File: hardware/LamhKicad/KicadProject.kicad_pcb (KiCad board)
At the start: 2 copper layers, 60 x 60 mm, 44 parts, among them J1 JTAG-10 PIN, J2 436500303, J3 436500303, J4 436500303, J5 ESQ-110-X-X-D, J6 436500303, U1 TJA1051T-3, U2 PCA9685PW_112, U3 TLV70433DBVT, U4 STM32F072C8Tx

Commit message: ready to route
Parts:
- added C16: 1000uf 16v, Capacitor_THT:CP_Radial_D10.0mm_P5.00mm, F.Cu at (184.0, 81.0)
- added C18: 1000uf 16v, Capacitor_THT:CP_Radial_D10.0mm_P5.00mm, F.Cu at (173.1, 90.2)
- added C19: 1000uf 16v, Capacitor_THT:CP_Radial_D10.0mm_P5.00mm, F.Cu at (194.8, 81.2)
- added C20: 1000uf 16v, Capacitor_THT:CP_Radial_D10.0mm_P5.00mm, F.Cu at (173.1, 101.0)
- moved R2 29.4 mm to (196.0, 90.9), turned to 90 degrees
- moved R1 25.8 mm to (197.0, 90.9), turned to 90 degrees
- moved R6 19.6 mm to (194.0, 90.9)
- moved R3 11.8 mm to (195.0, 90.9)
- moved JP1 10.1 mm to (204.2, 94.8)
- moved JP2 9.91 mm to (207.7, 95.5)
- moved JP3 9.91 mm to (204.2, 97.5)
- moved JP4 9.91 mm to (207.7, 98.2)
- moved R7 9.45 mm to (199.5, 102.2)
- moved R8 9.45 mm to (199.8, 101.2)
- moved C17 9.29 mm to (200.9, 99.6)
- moved R11 9.29 mm to (196.8, 100.5)
- moved U2 9.29 mm to (195.5, 96.0)
- moved C8 3.33 mm to (185.2, 101.0)
- moved C10 3.20 mm to (190.0, 112.4)
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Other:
- copper layers 2 -> 4

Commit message: Changes
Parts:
- moved C12 40.9 mm to (187.5, 94.6)
- moved C13 40.9 mm to (187.5, 96.1)
- moved C14 40.9 mm to (187.5, 98.0)
- moved C15 40.9 mm to (187.5, 100.0)
- moved R13 33.8 mm to (201.5, 97.0)
- moved R12 32.9 mm to (201.5, 96.0)
- moved R10 30.0 mm to (201.5, 95.0)
- moved R9 29.0 mm to (201.5, 94.0)
- moved C4 18.0 mm to (204.0, 110.0)
- moved C3 17.7 mm to (204.0, 108.5)
- moved C1 15.9 mm to (204.0, 107.1)
- moved C11 12.7 mm to (190.7, 112.4), turned to 0 degrees
- moved C10 12.7 mm to (184.3, 101.0)
- moved C9 9.53 mm to (190.7, 113.4), turned to 0 degrees
- moved C8 4.93 mm to (181.8, 104.5), turned to -90 degrees
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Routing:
- added copper zone on B.Cu, net GND
- added copper zone on F.Cu, net GND
- added copper zone on In1.Cu, net GND
- added copper zone on In2.Cu, net GND

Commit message: fixed the connector
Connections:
- J5 pad 12: NRST4 -> SWCLK4
- J5 pad 17: SWCLK -> NRST
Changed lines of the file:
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@@
 	(net 82 "Net-(JP3-B)")
 	(net 83 "Net-(JP4-B)")
+	(net 84 "NRST")
+	(net 85 "SWCLK4")
 	(footprint "Capacitor_SMD:C_0402_1005Metric"
 		(layer "F.Cu")
@@
 			(layers "*.Cu" "*.Mask")
 			(remove_unused_layers no)
-			(net 20 "NRST4")
+			(net 85 "SWCLK4")
 			(pinfunction "12")
 			(pintype "passive")
@@
 			(layers "*.Cu" "*.Mask")
 			(remove_unused_layers no)
-			(net 25 "SWCLK")
+			(net 84 "NRST")
 			(pinfunction "17")
 			(pintype "passive")

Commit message: minor changes
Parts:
- added R14: 10kΩ, Resistor_SMD:R_0402_1005Metric, F.Cu at (186.2, 101.0)
- added R15: 10kΩ, Resistor_SMD:R_0402_1005Metric, F.Cu at (179.0, 108.2)
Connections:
- U4 pad 44: unconnected-(U4-BOOT0-Pad44) -> Net-(U4-BOOT0)
- U4 pad 7: NRST4 -> NRST

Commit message: minor changes
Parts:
- removed R15: 10kΩ, Resistor_SMD:R_0402_1005Metric
- added C21: 100nF, Capacitor_SMD:C_0402_1005Metric, F.Cu at (184.2, 109.7)
- added C27: 8pF, Capacitor_SMD:C_0402_1005Metric, F.Cu at (181.2, 102.0)
- added C28: 8pF, Capacitor_SMD:C_0402_1005Metric, F.Cu at (180.2, 107.2)
- added G***: LOGO, LOGO, F.Cu at (196.3, 111.0)
- added G***: LOGO, LOGO, F.Cu at (185.8, 93.5)
- added XTAL1: NX3225GD-8MHZ-STD-CRA-3, footprints:XTAL_NX3225GD-8MHZ-STD-CRA-3_NDK, F.Cu at (181.2, 104.5)
- moved C12 14.8 mm to (182.0, 108.3), turned to 180 degrees
- moved R7 14.4 mm to (185.7, 98.2), turned to 0 degrees
- moved C13 14.3 mm to (182.0, 109.3), turned to 180 degrees
- moved R8 11.1 mm to (188.8, 99.2)
- moved C3 10.7 mm to (194.3, 104.0), turned to 90 degrees
- moved C4 10.6 mm to (195.3, 104.0), turned to 90 degrees
- moved C14 5.66 mm to (192.7, 100.2)
- moved C15 5.36 mm to (192.7, 101.2)
- moved C8 4.29 mm to (183.4, 100.5), turned to 90 degrees
- moved C7 4.26 mm to (182.4, 100.5), turned to 90 degrees
- moved C1 3.75 mm to (200.3, 107.2), turned to 180 degrees
- moved R6 2.85 mm to (191.2, 90.7), turned to 0 degrees
- moved C9 2.71 mm to (190.6, 110.7), turned to 180 degrees
- moved R14 2.48 mm to (187.2, 98.7), turned to 90 degrees
- moved U1 2.32 mm to (199.5, 103.9)
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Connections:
- J1 pad 1: NRST4 -> NRST
- J1 pad 2: SWCLK -> SWCLK4
- J5 pad 16: CAN_o+ -> CAN_+
- J5 pad 18: CAN_o- -> CAN_-
- R1 pad 1: Net-(J2-Pad1) -> Net-(J4-Pad1)
- R2 pad 1: Net-(J3-Pad1) -> Net-(J6-Pad1)
- R2 pad 2: Net-(U2-LED1) -> Net-(U2-LED2)
- R3 pad 1: Net-(J4-Pad1) -> Net-(J2-Pad1)
- R3 pad 2: Net-(U2-LED2) -> Net-(U2-LED4)
- R6 pad 1: Net-(J6-Pad1) -> Net-(J3-Pad1)
- R6 pad 2: Net-(U2-LED3) -> Net-(U2-LED6)
- U1 pad 1: CAN_+ -> CAN_e+
- U1 pad 4: CAN_- -> CAN_e-
- U2 pad 10: unconnected-(U2-LED4-Pad10) -> Net-(U2-LED4)
- U2 pad 12: unconnected-(U2-LED6-Pad12) -> Net-(U2-LED6)
- U2 pad 7: Net-(U2-LED1) -> unconnected-(U2-LED1-Pad7)
- U2 pad 9: Net-(U2-LED3) -> unconnected-(U2-LED3-Pad9)
- U4 pad 11: CS -> unconnected-(U4-PA1-Pad11)
- U4 pad 12: OE -> unconnected-(U4-PA2-Pad12)
- U4 pad 13: RESET -> unconnected-(U4-PA3-Pad13)
- U4 pad 14: ADC -> unconnected-(U4-PA4-Pad14)
- U4 pad 15: CLK -> unconnected-(U4-PA5-Pad15)
- U4 pad 16: MISO -> unconnected-(U4-PA6-Pad16)
- U4 pad 17: MOSI -> unconnected-(U4-PA7-Pad17)
- U4 pad 3: SWCLK -> SWCLK4
- U4 pad 32: CAN_- -> CAN_e-
- U4 pad 33: CAN_+ -> CAN_e+
- U4 pad 5: unconnected-(U4-PF0-Pad5) -> Net-(U4-PF0)
- U4 pad 6: unconnected-(U4-PF1-Pad6) -> Net-(U4-PF1)
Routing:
- net 3.3V: track 1.52 -> 122.9 mm, vias 0 -> 9
- net NRST: track 0.00 -> 69.0 mm, vias 0 -> 1
- net SWCLK4: track 0.00 -> 50.1 mm, vias 0 -> 1
- net SWDIO: track 0.00 -> 46.8 mm, vias 0 -> 1
- net Net-(J3-Pad1): track 0.00 -> 31.4 mm
- net Net-(J2-Pad1): track 0.00 -> 28.7 mm
- net Net-(J6-Pad1): track 0.00 -> 25.5 mm
- net SCL: track 0.00 -> 19.3 mm, vias 0 -> 2
- net GND: track 1.56 -> 19.9 mm, vias 0 -> 50
- net SDA: track 0.00 -> 17.8 mm, vias 0 -> 2
- net Net-(J4-Pad1): track 0.00 -> 17.7 mm
- net Net-(JP4-B): track 0.00 -> 14.1 mm
- net Net-(JP2-B): track 0.00 -> 10.6 mm
- net Net-(JP3-B): track 0.00 -> 9.05 mm
- net CAN_-: track 3.72 -> 12.0 mm
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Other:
- board text added: "Lamh - v1.0"

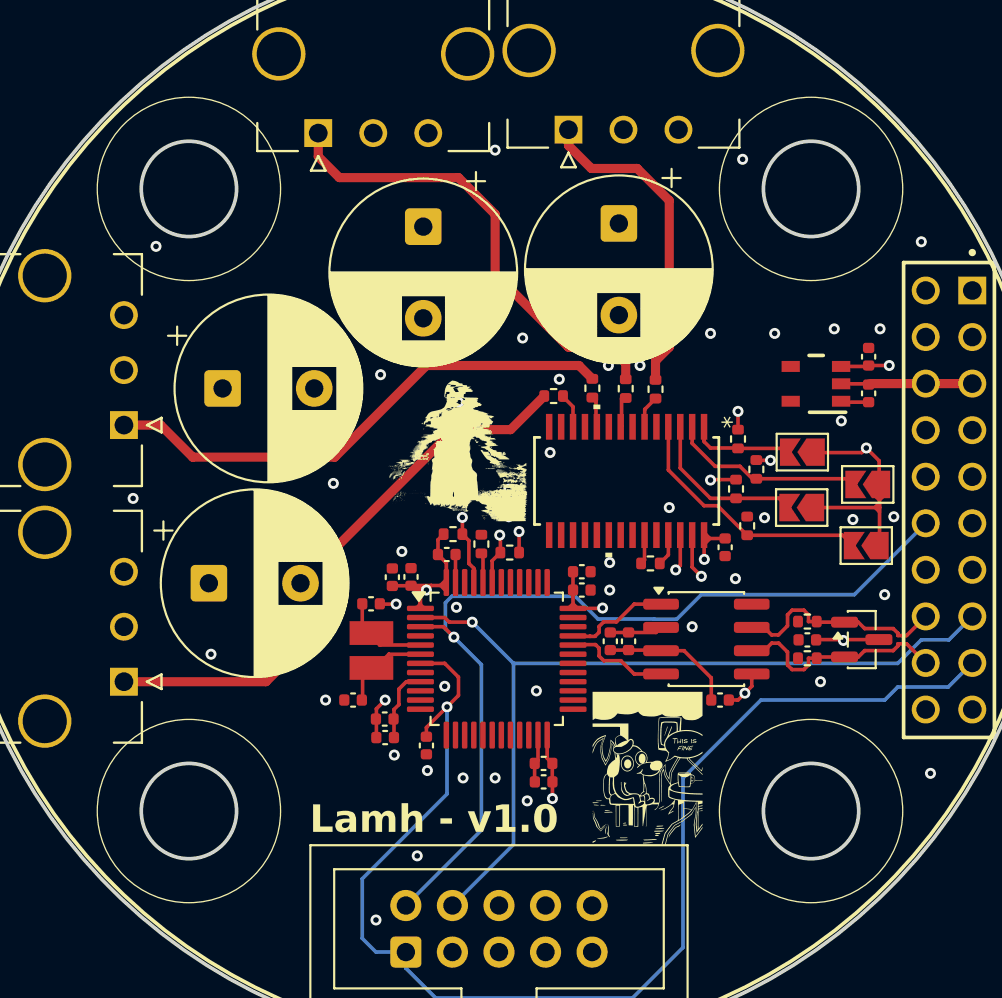
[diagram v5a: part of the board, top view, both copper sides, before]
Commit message: thermal expansion vias
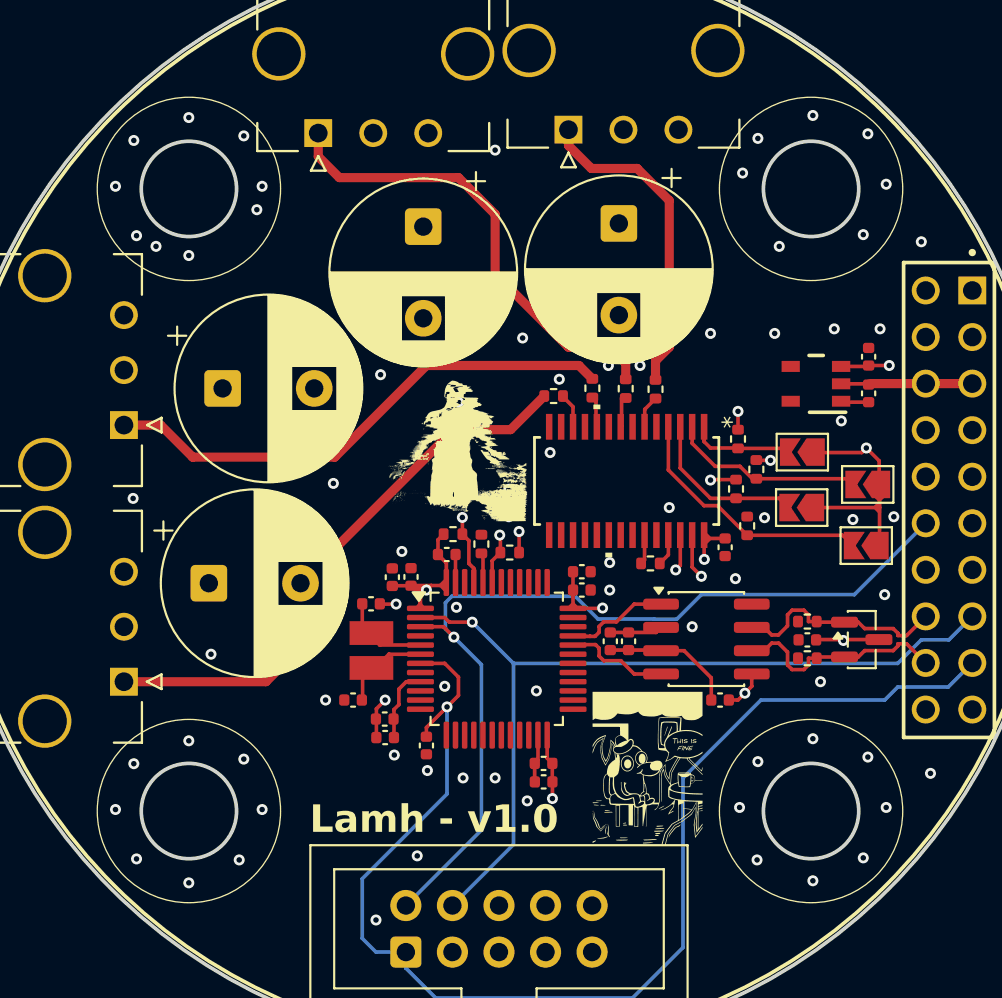
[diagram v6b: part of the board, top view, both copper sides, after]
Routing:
- net GND: track 19.9 -> 24.8 mm, vias 50 -> 80

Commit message: mockup done, must finish routing
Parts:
- added 3v3: S2761-46R, footprints:HARWIN_S2761-46R, F.Cu at (267.2, 103.8)
- added C+1: S2761-46R, footprints:HARWIN_S2761-46R, F.Cu at (267.2, 106.3)
- added C-1: S2761-46R, footprints:HARWIN_S2761-46R, F.Cu at (267.2, 108.9)
- added C22: 22uf, Capacitor_SMD:C_0402_1005Metric, F.Cu at (250.1, 107.4)
- added C23: 22uf, Capacitor_SMD:C_0402_1005Metric, F.Cu at (250.1, 109.4)
- added C24: 0.1uf, Capacitor_SMD:C_0402_1005Metric, F.Cu at (250.1, 111.4)
- added C25: 1uf, Capacitor_SMD:C_0402_1005Metric, F.Cu at (253.0, 103.5)
- added C26: 22uf, Capacitor_SMD:C_0402_1005Metric, F.Cu at (253.0, 105.5)
- added C29: 22uf, Capacitor_SMD:C_0402_1005Metric, F.Cu at (253.0, 107.4)
- added C30: 22uf, Capacitor_SMD:C_0402_1005Metric, F.Cu at (253.0, 109.4)
- added C31: 22uf, Capacitor_SMD:C_0402_1005Metric, F.Cu at (253.0, 111.4)
- added C32: 4.7uf, Capacitor_SMD:C_0402_1005Metric, F.Cu at (255.9, 103.5)
- added C33: 4.7uf, Capacitor_SMD:C_0402_1005Metric, F.Cu at (255.9, 105.5)
- added C34: 10uf, Capacitor_SMD:C_0402_1005Metric, F.Cu at (255.9, 107.4)
- added G***: LOGO, LOGO, F.Cu at (188.5, 115.8)
- added GND1: S2761-46R, footprints:HARWIN_S2761-46R, F.Cu at (267.2, 111.4)
- added R15: 10kΩ, Resistor_SMD:R_0402_1005Metric, F.Cu at (247.2, 103.5)
- added R16: 53.6kΩ, Resistor_SMD:R_0402_1005Metric, F.Cu at (247.2, 105.5)
- added R17: 0Ω, Resistor_SMD:R_0402_1005Metric, F.Cu at (247.2, 107.5)
- added R18: 0Ω, Resistor_SMD:R_0402_1005Metric, F.Cu at (247.2, 109.5)
- added R19: 499kΩ, Resistor_SMD:R_0402_1005Metric, F.Cu at (247.2, 111.5)
- added R20: 100kΩ, Resistor_SMD:R_0402_1005Metric, F.Cu at (247.2, 113.5)
- added R21: 33.2kΩ, Resistor_SMD:R_0402_1005Metric, F.Cu at (247.2, 115.5)
- added S1: S2761-46R, footprints:HARWIN_S2761-46R, F.Cu at (267.2, 114.0)
- added S2: S2761-46R, footprints:HARWIN_S2761-46R, F.Cu at (270.6, 103.8)
- added S3: S2761-46R, footprints:HARWIN_S2761-46R, F.Cu at (270.6, 106.3)
- added S4: S2761-46R, footprints:HARWIN_S2761-46R, F.Cu at (270.6, 108.9)
- added VR1: LT3045EDD_PBF, footprints:SON50P300X300X80-11N, F.Cu at (206.2, 90.5)
- C2: value 100nF -> 39pf
- C5: value 100uF -> 0.1uf
- J1: value JTAG-10 PIN -> 5023860570; footprint Connector_IDC:IDC-Header_2x05_P2.54mm_Vertical -> footprints:MOLEX_5023860570
- U3: value TLV70433DBVT -> MPM3650CGQW-P; footprint footprints:DBV0005A_N -> footprints:QFN-24_MPM3650_MNP
- moved U3 57.4 mm to (260.4, 106.6), turned to 0 degrees
- moved C5 45.1 mm to (250.1, 105.5), turned to 0 degrees
- moved C2 43.7 mm to (250.1, 103.5), turned to 0 degrees
- moved G*** 34.1 mm to (164.0, 119.8)
- moved J1 5.10 mm to (188.0, 122.5), turned to 180 degrees
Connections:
- C2 pad 1: 5V_LOGIC -> Net-(VR1-EN/UV)
- C2 pad 2: GND -> Net-(C2-Pad2)
- C5 pad 2: 3.3V -> 5V_LOGIC
- J1 pad 1: NRST -> SWCLK
- J1 pad 2: SWCLK4 -> SWDIO
- J1 pad 3: unconnected-(J1-Pin_3-Pad3) -> NRST
- J1 pad 4: SWDIO -> 3.3V
- J5 pad 01: 5v_SERVO -> GND
- J5 pad 02: 5v_SERVO -> GND
- J5 pad 03: GND -> 5v_SERVO
- J5 pad 04: GND -> 5v_SERVO
- J5 pad 05: 5V_LOGIC -> 5v_SERVO
- J5 pad 06: 5V_LOGIC -> 5v_SERVO
- J5 pad 07: GND -> 5v_SERVO
- J5 pad 08: GND -> 5v_SERVO
- J5 pad 09: unconnected-(J5-Pad09) -> GND
- J5 pad 10: unconnected-(J5-Pad10) -> GND
- J5 pad 11: unconnected-(J5-Pad11) -> 5V_LOGIC
- J5 pad 12: SWCLK4 -> 5V_LOGIC
- J5 pad 13: unconnected-(J5-Pad13) -> GND
- J5 pad 15: SWDIO -> GND
- J5 pad 17: NRST -> GND
- U3 pad 2: 5V_LOGIC -> GND
- U3 pad 3: 3.3V -> GND
- U3 pad 4: unconnected-(U3-NC-Pad4) -> GND
- U3 pad 5: unconnected-(U3-NC-Pad5) -> GND
- U4 pad 3: SWCLK4 -> SWCLK
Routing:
- net SWCLK4: track 50.1 -> 0.00 mm, vias 1 -> 0
- net (no net): track 0.00 -> 50.1 mm
- net Net-(VR1-EN/UV): track 0.00 -> 17.9 mm
- net 5v_SERVO: track 0.00 -> 7.19 mm
- net 5V_LOGIC: track 7.19 -> 0.00 mm
- net GND: track 24.8 -> 26.5 mm
- net Net-(VR1-SET): track 0.00 -> 1.52 mm
- net SWCLK: vias 0 -> 1
- added copper zone on In3.Cu, net GND
- removed copper zone on In1.Cu, net GND
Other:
- outline, holes or cut-outs redrawn
- copper layers 4 -> 6
- board text added: "SWCLK SWDIO NRST 3v3 GND"
- board text added: "lamh-v1.0"
- board text removed: "Lamh - v1.0"
